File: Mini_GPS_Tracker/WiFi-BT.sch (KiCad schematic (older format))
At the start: 1 part, among them IC4 NINA-W102

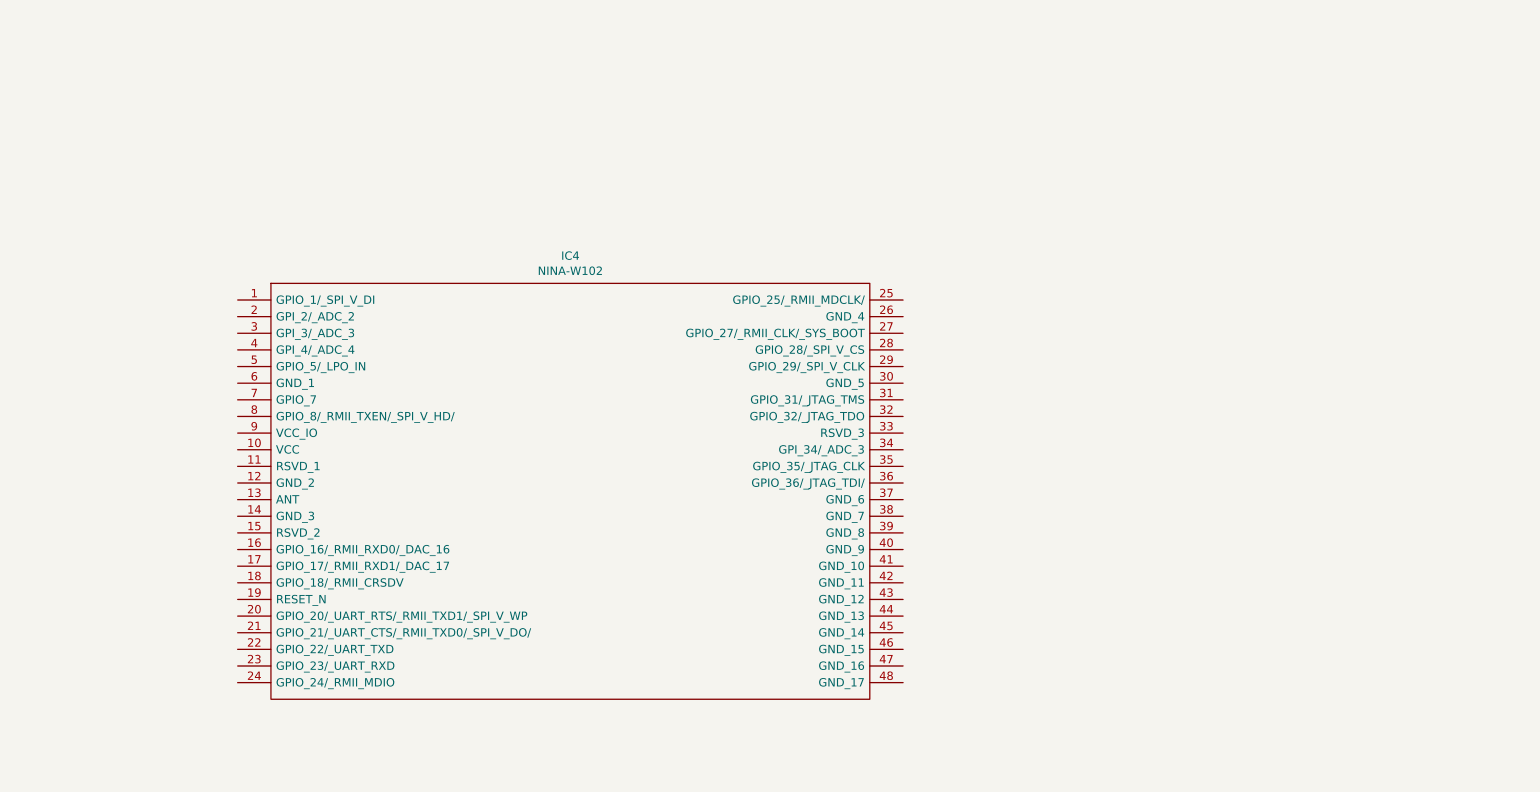
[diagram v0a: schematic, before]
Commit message: Add files via upload
Breaking out more pins
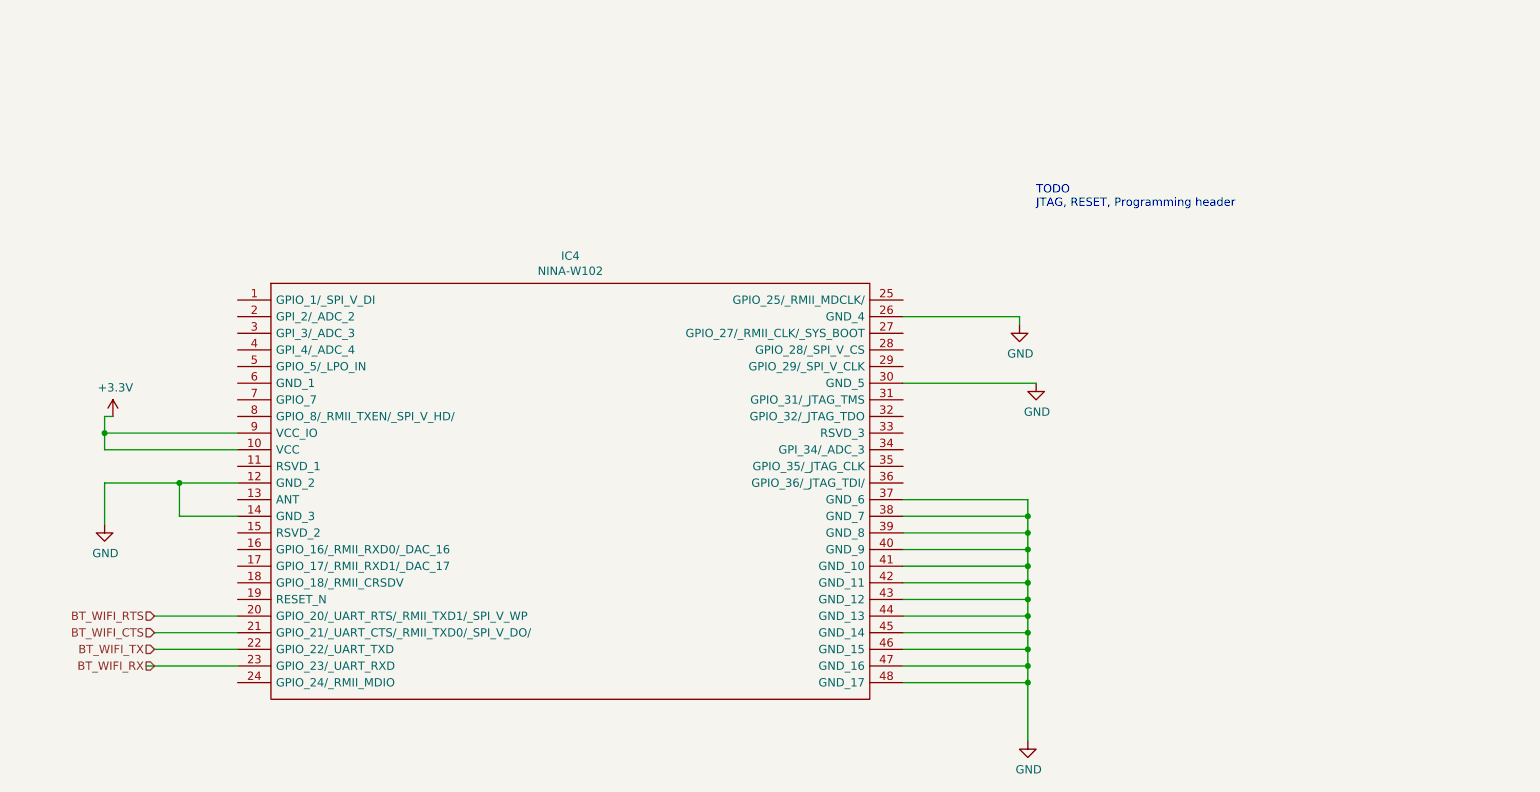
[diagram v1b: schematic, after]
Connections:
- net +3V3: now reaches IC4.10 (VCC)
- net +3V3: now also IC4.9 (VCC_IO)
- net GND: now reaches IC4.12 (GND_2)
- net GND: now also IC4.14 (GND_3), IC4.26 (GND_4), IC4.30 (GND_5), IC4.37 (GND_6), IC4.38 (GND_7), IC4.39 (GND_8), IC4.40 (GND_9), IC4.41 (GND_10), IC4.42 (GND_11), IC4.43 (GND_12), IC4.44 (GND_13), IC4.45 (GND_14), IC4.46 (GND_15), IC4.47 (GND_16), IC4.48 (GND_17)
- net BT_WIFI_RTS: now reaches IC4.20 (GPIO_20/_UART_RTS/_RMII_TXD1/_SPI_V_WP)
- net BT_WIFI_CTS: now reaches IC4.21 (GPIO_21/_UART_CTS/_RMII_TXD0/_SPI_V_DO/)
- net BT_WIFI_TX: now reaches IC4.22 (GPIO_22/_UART_TXD)
- net BT_WIFI_RX: now reaches IC4.23 (GPIO_23/_UART_RXD)
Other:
- note added: "TODO\nJTAG, RESET, Programming header"
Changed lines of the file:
@@
 	1    0    0    -1
 $EndComp
+$Comp
+L power:GND #PWR?
+U 1 1 5EB641E1
+P 8250 5100
+F 0 "#PWR?" H 8250 4850 50  0001 C CNN
+F 1 "GND" H 8255 4927 50  0000 C CNN
+F 2 "" H 8250 5100 50  0001 C CNN
+F 3 "" H 8250 5100 50  0001 C CNN
+	1    8250 5100
+	1    0    0    -1
+$EndComp
+Wire Wire Line
+	7500 3650 8250 3650
+Wire Wire Line
+	8250 3650 8250 3750
+Wire Wire Line
+	7500 3750 8250 3750
+Connection ~ 8250 3750
+Wire Wire Line
+	8250 3750 8250 3850
+Wire Wire Line
+	7500 3850 8250 3850
+Connection ~ 8250 3850
+Wire Wire Line
+	8250 3850 8250 3950
+Wire Wire Line
+	7500 3950 8250 3950
+Connection ~ 8250 3950
+Wire Wire Line
+	8250 3950 8250 4050
+Wire Wire Line
+	7500 4050 8250 4050
+Connection ~ 8250 4050
+Wire Wire Line
+	8250 4050 8250 4150
+Wire Wire Line
+	7500 4150 8250 4150
+Connection ~ 8250 4150
+Wire Wire Line
+	8250 4150 8250 4250
+Wire Wire Line
+	7500 4250 8250 4250
+Connection ~ 8250 4250
+Wire Wire Line
+	8250 4250 8250 4350
+Wire Wire Line
+	7500 4350 8250 4350
+Connection ~ 8250 4350
+Wire Wire Line
+	8250 4350 8250 4450
+Wire Wire Line
+	7500 4450 8250 4450
+Connection ~ 8250 4450
+Wire Wire Line
+	8250 4450 8250 4550
+Wire Wire Line
+	7500 4550 8250 4550
+Connection ~ 8250 4550
+Wire Wire Line
+	8250 4550 8250 4650
+Wire Wire Line
+	7500 4650 8250 4650
+Connection ~ 8250 4650
+Wire Wire Line
+	7500 4750 8250 4750
+Wire Wire Line
+	8250 4650 8250 4750
+Connection ~ 8250 4750
+Wire Wire Line
+	8250 4750 8250 5100
+$Comp
+L power:GND #PWR?
+U 1 1 5EB65974
+P 8200 2600
+F 0 "#PWR?" H 8200 2350 50  0001 C CNN
+F 1 "GND" H 8205 2427 50  0000 C CNN
+F 2 "" H 8200 2600 50  0001 C CNN
+F 3 "" H 8200 2600 50  0001 C CNN
+	1    8200 2600
+	1    0    0    -1
+$EndComp
+Wire Wire Line
+	7500 2550 8200 2550
+Wire Wire Line
+	8200 2550 8200 2600
+$Comp
+L power:GND #PWR?
+U 1 1 5EB6622F
+P 8300 2950
+F 0 "#PWR?" H 8300 2700 50  0001 C CNN
+F 1 "GND" H 8305 2777 50  0000 C CNN
+F 2 "" H 8300 2950 50  0001 C CNN
+F 3 "" H 8300 2950 50  0001 C CNN
+	1    8300 2950
+	1    0    0    -1
+$EndComp
+Wire Wire Line
+	7500 2950 8300 2950
+$Comp
+L power:GND #PWR?
+U 1 1 5EB66F6E
+P 2700 3800
+F 0 "#PWR?" H 2700 3550 50  0001 C CNN
+F 1 "GND" H 2705 3627 50  0000 C CNN
+F 2 "" H 2700 3800 50  0001 C CNN
+F 3 "" H 2700 3800 50  0001 C CNN
+	1    2700 3800
+	1    0    0    -1
+$EndComp
+Wire Wire Line
+	3500 3550 3150 3550
+Wire Wire Line
+	2700 3550 2700 3800
+$Comp
+L power:+3.3V #PWR?
+U 1 1 5EB67963
+P 2750 3150
+F 0 "#PWR?" H 2750 3000 50  0001 C CNN
+F 1 "+3.3V" H 2765 3323 50  0000 C CNN
+F 2 "" H 2750 3150 50  0001 C CNN
+F 3 "" H 2750 3150 50  0001 C CNN
+	1    2750 3150
+	1    0    0    -1
+$EndComp
+Wire Wire Line
+	3500 3350 2700 3350
+Wire Wire Line
+	2700 3150 2750 3150
+Wire Wire Line
+	3500 3250 2700 3250
+Wire Wire Line
+	2700 3150 2700 3250
+Connection ~ 2700 3250
+Wire Wire Line
+	2700 3250 2700 3350
+Wire Wire Line
+	3500 3750 3150 3750
+Wire Wire Line
+	3150 3750 3150 3550
+Connection ~ 3150 3550
+Wire Wire Line
+	3150 3550 2700 3550
+Text HLabel 3000 4550 0    50   Input ~ 0
+BT_WIFI_TX
+Text HLabel 3000 4650 0    50   Input ~ 0
+BT_WIFI_RX
+Text HLabel 3000 4350 0    50   Input ~ 0
+BT_WIFI_RTS
+Text HLabel 3000 4450 0    50   Input ~ 0
+BT_WIFI_CTS
+Wire Wire Line
+	3000 4350 3500 4350
+Wire Wire Line
+	3000 4450 3500 4450
+Wire Wire Line
+	3000 4550 3500 4550
+Wire Wire Line
+	2950 4650 3500 4650
+Text Notes 8300 1900 0    50   ~ 0
+TODO\nJTAG, RESET, Programming header
 $EndSCHEMATC

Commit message: Add files via upload
More changes - USB, WiFi/BT, Buzzer, Siren-LED Flasher
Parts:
- added C?: 10nF, symbol Device:C
- added J?: Conn_01x05_Male, symbol Connector:Conn_01x05_Male
- added R? (x2): 10K, symbol Device:R
- added SW? (x2): SW_Push, symbol Switch:SW_Push
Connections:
- net labels added: Boot, Reset, Reset_N
- wire segments 41 -> 71
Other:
- note removed: "TODO\nJTAG, RESET, Programming header"
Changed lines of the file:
@@
 Wire Wire Line
 	2950 4650 3500 4650
-Text Notes 8300 1900 0    50   ~ 0
-TODO\nJTAG, RESET, Programming header
+$Comp
+L Connector:Conn_01x05_Male J?
+U 1 1 5EB9F685
+P 9550 3400
+F 0 "J?" H 9658 3781 50  0000 C CNN
+F 1 "Conn_01x05_Male" H 9658 3690 50  0000 C CNN
+F 2 "" H 9550 3400 50  0001 C CNN
+F 3 "~" H 9550 3400 50  0001 C CNN
+	1    9550 3400
+	1    0    0    -1
+$EndComp
+Wire Wire Line
+	7500 3550 8950 3550
+Wire Wire Line
+	8950 3550 8950 3200
+Wire Wire Line
+	8950 3200 9550 3200
+Wire Wire Line
+	7500 3150 8750 3150
+Wire Wire Line
+	8750 3150 8750 3300
+Wire Wire Line
+	8750 3300 9550 3300
+Wire Wire Line
+	7500 3450 8750 3450
+Wire Wire Line
+	8750 3450 8750 3400
+Wire Wire Line
+	8750 3400 9600 3400
+Wire Wire Line
+	7500 3050 9150 3050
+Wire Wire Line
+	9150 3050 9150 3500
+Wire Wire Line
+	9150 3500 9550 3500
+Text GLabel 9300 3950 0    50   Input ~ 0
+Reset
+Wire Wire Line
+	9300 3950 9450 3950
+Wire Wire Line
+	9450 3950 9450 3600
+Wire Wire Line
+	9450 3600 9550 3600
+Text HLabel 2900 4250 0    50   Input ~ 0
+Reset_N
+Wire Wire Line
+	2900 4250 3500 4250
+Text HLabel 8900 2650 2    50   Input ~ 0
+Boot
+Wire Wire Line
+	7500 2650 8900 2650
+$Comp
+L power:GND #PWR?
+U 1 1 5EBA8D2B
+P 2750 2600
+F 0 "#PWR?" H 2750 2350 50  0001 C CNN
+F 1 "GND" H 2755 2427 50  0000 C CNN
+F 2 "" H 2750 2600 50  0001 C CNN
+F 3 "" H 2750 2600 50  0001 C CNN
+	1    2750 2600
+	1    0    0    -1
+$EndComp
+$Comp
+L Switch:SW_Push SW?
+U 1 1 5EBAA095
+P 9100 1550
+F 0 "SW?" H 9100 1835 50  0000 C CNN
+F 1 "SW_Push" H 9100 1744 50  0000 C CNN
+F 2 "" H 9100 1750 50  0001 C CNN
+F 3 "~" H 9100 1750 50  0001 C CNN
+	1    9100 1550
+	1    0    0    -1
+$EndComp
+$Comp
+L power:GND #PWR?
+U 1 1 5EBAA700
+P 9300 1650
+F 0 "#PWR?" H 9300 1400 50  0001 C CNN
+F 1 "GND" H 9305 1477 50  0000 C CNN
+F 2 "" H 9300 1650 50  0001 C CNN
+F 3 "" H 9300 1650 50  0001 C CNN
+	1    9300 1650
+	1    0    0    -1
+$EndComp
+Wire Wire Line
+	9300 1550 9300 1650
+$Comp
+L Device:R R?
+U 1 1 5EBABFD7
+P 8700 1400
+F 0 "R?" H 8770 1446 50  0000 L CNN
+F 1 "10K" H 8770 1355 50  0000 L CNN
+F 2 "" V 8630 1400 50  0001 C CNN
+F 3 "~" H 8700 1400 50  0001 C CNN
+	1    8700 1400
+	1    0    0    -1
+$EndComp
+$Comp
+L power:+3.3V #PWR?
+U 1 1 5EBAC3FF
+P 8700 1200
+F 0 "#PWR?" H 8700 1050 50  0001 C CNN
+F 1 "+3.3V" H 8715 1373 50  0000 C CNN
+F 2 "" H 8700 1200 50  0001 C CNN
+F 3 "" H 8700 1200 50  0001 C CNN
+	1    8700 1200
+	1    0    0    -1
+$EndComp
+Wire Wire Line
+	8700 1200 8700 1250
+Text GLabel 8250 1550 0    50   Input ~ 0
+Boot
+$Comp
+L Switch:SW_Push SW?
+U 1 1 5EBAFBBA
+P 10950 1550
+F 0 "SW?" H 10950 1835 50  0000 C CNN
+F 1 "SW_Push" H 10950 1744 50  0000 C CNN
+F 2 "" H 10950 1750 50  0001 C CNN
+F 3 "~" H 10950 1750 50  0001 C CNN
+	1    10950 1550
+	1    0    0    -1
+$EndComp
+$Comp
+L power:GND #PWR?
+U 1 1 5EBAFBC0
+P 11150 1650
+F 0 "#PWR?" H 11150 1400 50  0001 C CNN
+F 1 "GND" H 11155 1477 50  0000 C CNN
+F 2 "" H 11150 1650 50  0001 C CNN
+F 3 "" H 11150 1650 50  0001 C CNN
+	1    11150 1650
+	1    0    0    -1
+$EndComp
+Wire Wire Line
+	11150 1550 11150 1650
+$Comp
+L Device:R R?
+U 1 1 5EBAFBC7
+P 10500 1400
+F 0 "R?" H 10570 1446 50  0000 L CNN
+F 1 "10K" H 10570 1355 50  0000 L CNN
+F 2 "" V 10430 1400 50  0001 C CNN
+F 3 "~" H 10500 1400 50  0001 C CNN
+	1    10500 1400
+	1    0    0    -1
+$EndComp
+$Comp
+L power:+3.3V #PWR?
+U 1 1 5EBAFBCE
+P 10500 1200
+F 0 "#PWR?" H 10500 1050 50  0001 C CNN
+F 1 "+3.3V" H 10515 1373 50  0000 C CNN
+F 2 "" H 10500 1200 50  0001 C CNN
+F 3 "" H 10500 1200 50  0001 C CNN
+	1    10500 1200
+	1    0    0    -1
+$EndComp
+Wire Wire Line
+	10500 1200 10500 1250
+Text GLabel 10050 1550 0    50   Input ~ 0
+Reset_N
+Wire Wire Line
+	3500 2950 3100 2950
+Wire Wire Line
+	3100 2950 3100 2500
+Wire Wire Line
+	3100 2500 2750 2500
+Wire Wire Line
+	2750 2500 2750 2600
+$Comp
+L Device:C C?
+U 1 1 5EBB2A66
+P 10150 1700
+F 0 "C?" H 10265 1746 50  0000 L CNN
+F 1 "10nF" H 10265 1655 50  0000 L CNN
+F 2 "" H 10188 1550 50  0001 C CNN
+F 3 "~" H 10150 1700 50  0001 C CNN
+	1    10150 1700
+	1    0    0    -1
+$EndComp
+$Comp
+L power:GND #PWR?
+U 1 1 5EBB2DE1
+P 10150 1850
+F 0 "#PWR?" H 10150 1600 50  0001 C CNN
+F 1 "GND" H 10155 1677 50  0000 C CNN
+F 2 "" H 10150 1850 50  0001 C CNN
+F 3 "" H 10150 1850 50  0001 C CNN
+	1    10150 1850
+	1    0    0    -1
+$EndComp
+Wire Wire Line
+	10050 1550 10150 1550
+Connection ~ 10500 1550
+Connection ~ 10150 1550
+Wire Wire Line
+	10150 1550 10500 1550
+Wire Wire Line
+	10500 1550 10750 1550
+Wire Wire Line
+	8250 1550 8700 1550
+Connection ~ 8700 1550
+Wire Wire Line
+	8700 1550 8900 1550
 $EndSCHEMATC

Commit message: Add files via upload
Added RFM95 board
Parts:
- removed R?: 10K, symbol Device:R
- removed SW?: SW_Push, symbol Switch:SW_Push
- added 10K? (x2): R, symbol Device:R
- added C?: 10nF, symbol Device:C
- added SW?: SW_DIP_x02, symbol Switch:SW_DIP_x02
- J?: value Conn_01x05_Male -> JTAG
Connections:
- net labels added: BT_WIFI_Boot0, BT_WIFI_Boot1, BT_WIFI_Reset_N
- net labels removed: Boot, Reset
- wire segments 71 -> 82
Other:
- moved on the sheet: C?, R?, SW?
